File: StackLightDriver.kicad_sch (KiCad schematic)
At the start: 57 parts, among them J1 B2B-XH-A, J10 B2B-XH-A, J11 PJ-102AH, J2 B2B-XH-A, J3 B2B-XH-A, J4 B2B-XH-A, J5 B2B-XH-A, J6 B2B-XH-A, J7 B2B-XH-A, J8 B2B-XH-A, J9 B2B-XH-A, P1 282837-2, P2 282837-2, P3 282837-2, P4 282837-2, U6 ESP32-S3-WROOM-1-N4

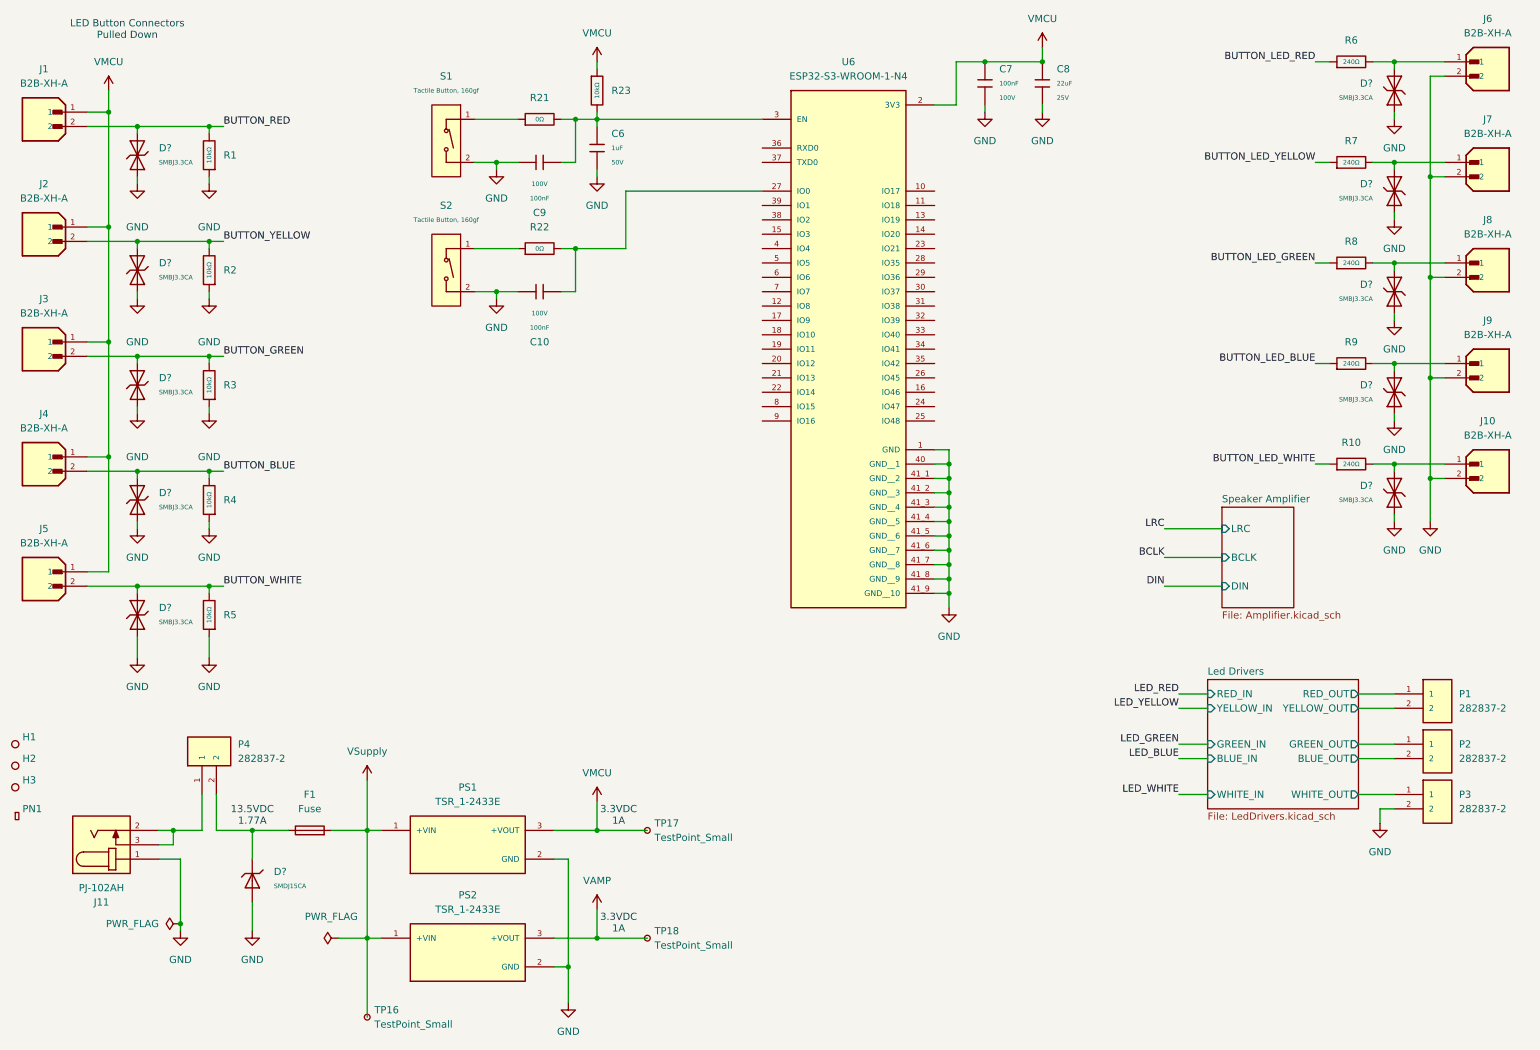
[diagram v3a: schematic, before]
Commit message: Rearranged ESP32 symbol, added note file
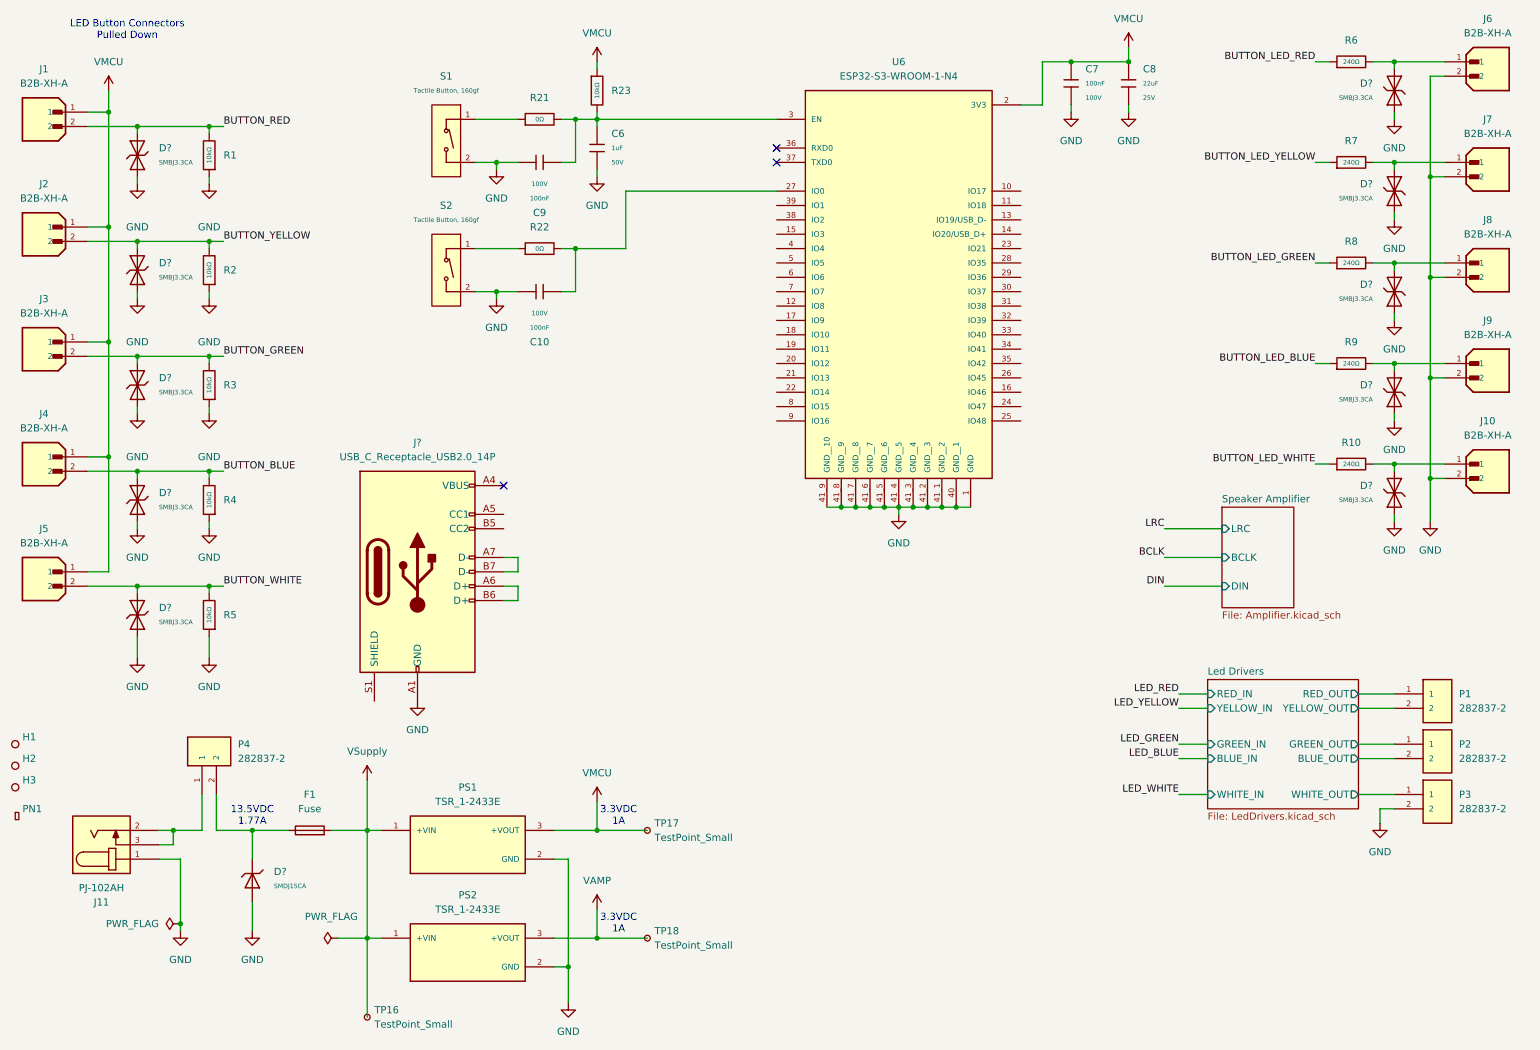
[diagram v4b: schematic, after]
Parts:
- added J?: USB_C_Receptacle_USB2.0_14P, symbol Connector:USB_C_Receptacle_USB2.0_14P
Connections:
- net GND: now also J?.A1 (GND), J?.A12 (GND), J?.B1 (GND), J?.B12 (GND)
- new net: J?.A4 (VBUS), J?.A9 (VBUS), J?.B4 (VBUS), J?.B9 (VBUS)
- new net: J?.A6 (D+), J?.B6 (D+)
- new net: J?.A7 (D-), J?.B7 (D-)
- no-connect marks 0 -> 3
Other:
- moved on the sheet: C7, C8, U6

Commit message: Added USB C connections and USB C TVS diodes
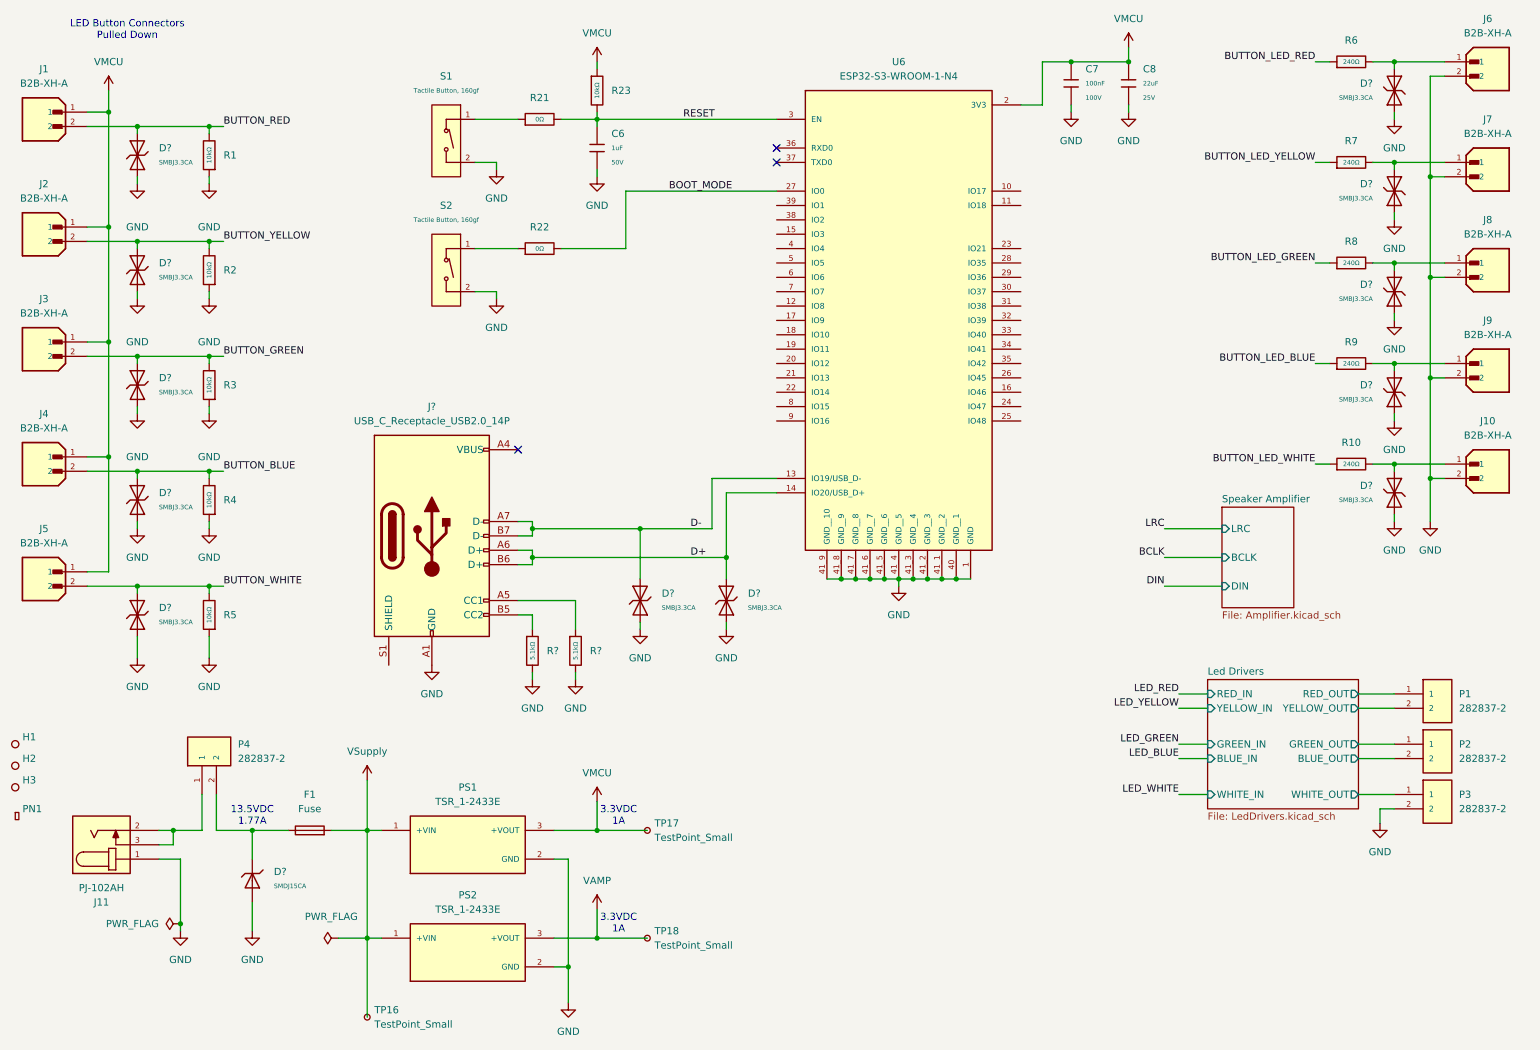
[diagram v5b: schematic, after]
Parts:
- removed C10, C9: 100nF, PCM_JLCPCB:C_0805, symbol PCM_JLCPCB-Capacitors:0805,100nF
- removed J?: USB_C_Receptacle_USB2.0_14P, symbol Connector:USB_C_Receptacle_USB2.0_14P
- added D? (x2): SMBJ3.3CA, PCM_JLCPCB:D_SMB, symbol PCM_JLCPCB-Diodes:TVS-Bi,SMBJ3.3CA
- added J?: USB_C_Receptacle_USB2.0_14P, symbol Project_symbols:USB_C_Receptacle_USB2.0_14P
- added R? (x2): 5.1kΩ, PCM_JLCPCB:R_0805, symbol PCM_JLCPCB-Resistors:0805,5.1kΩ
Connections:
- net GND: now also D?.1, D?.1, J?.A1 (GND), J?.A12 (GND), J?.B1 (GND), J?.B12 (GND), R?.2, R?.2
- net RESET: now reaches C6.1, R21.2, R23.2, U6.3 (EN)
- net D-: now reaches U6.13 (IO19/USB_D-)
- net D-: now also D?.2, J?.A7 (D-), J?.B7 (D-)
- net D+: now reaches U6.14 (IO20/USB_D+)
- net D+: now also D?.2, J?.A6 (D+), J?.B6 (D+)
- net BOOT_MODE: now reaches R22.2, U6.27 (IO0)
- new net: J?.A4 (VBUS), J?.A9 (VBUS), J?.B4 (VBUS), J?.B9 (VBUS)
- new net: J?.A5 (CC1), R?.1
- new net: J?.B5 (CC2), R?.1
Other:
- moved on the sheet: U6

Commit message: Added basic Littelfuse clip model, began laying out PCB
Still needs revisions to TVS diodes.
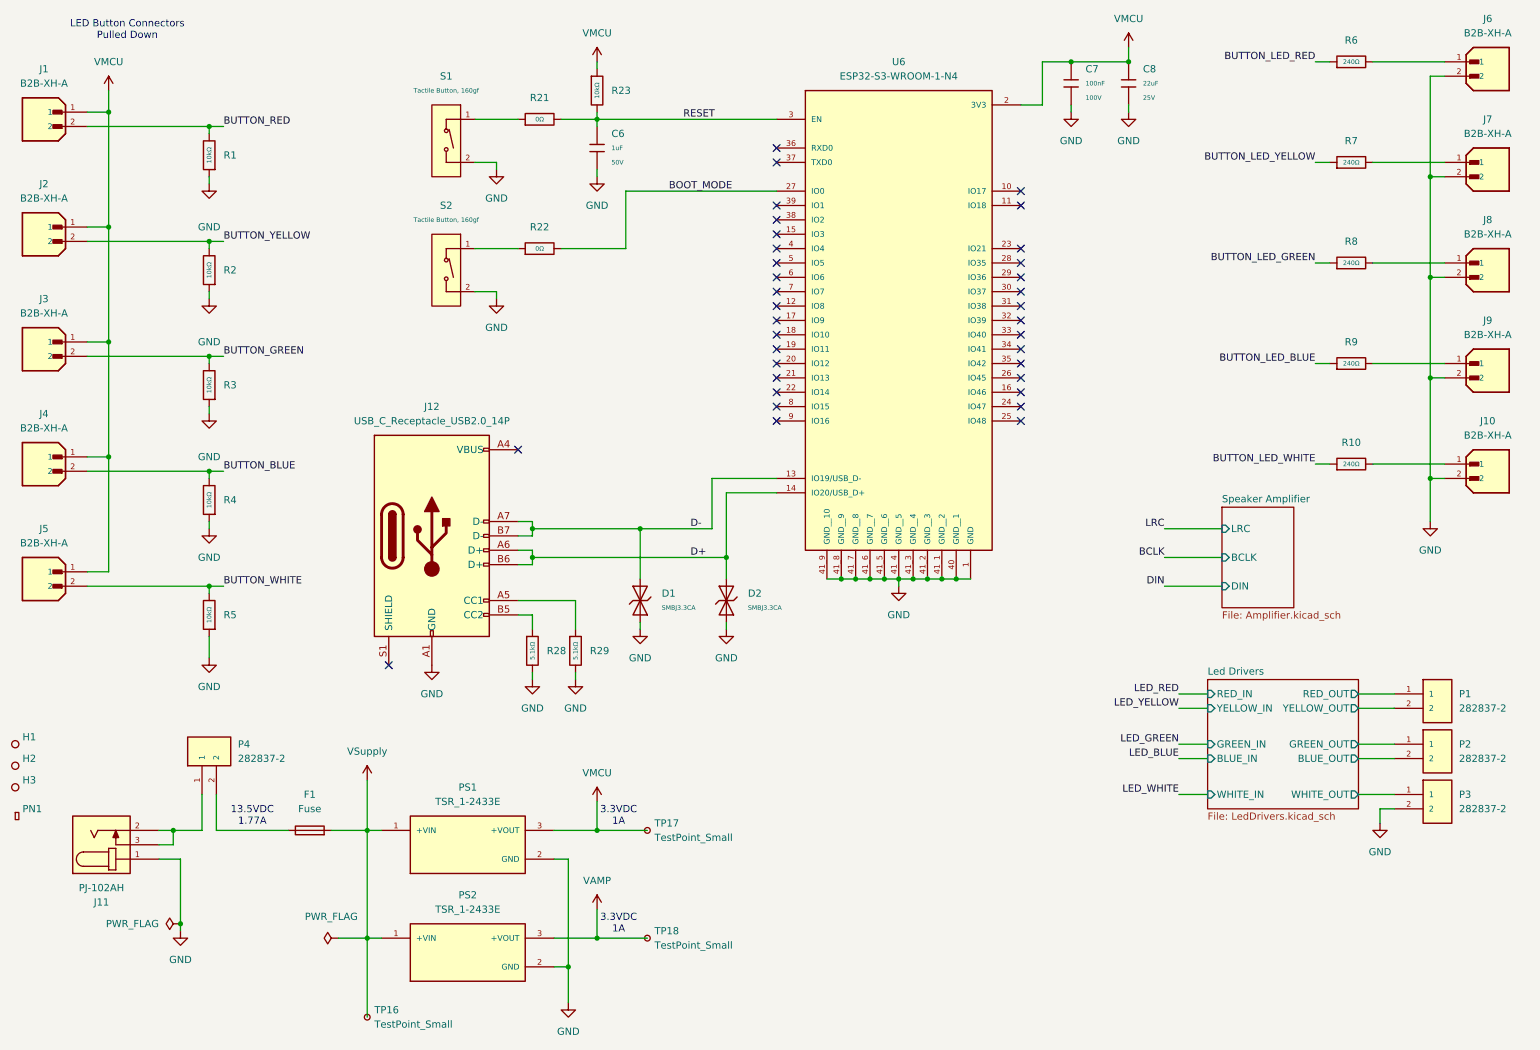
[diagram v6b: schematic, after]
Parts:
- removed D? (x10): SMBJ3.3CA, PCM_JLCPCB:D_SMB, symbol PCM_JLCPCB-Diodes:TVS-Bi,SMBJ3.3CA
- removed D?: SMDJ15CA, PCM_JLCPCB:D_SMC, symbol PCM_JLCPCB-Diodes:TVS-Uni,SMDJ15CA
- F1: footprint Fuse:Fuseholder_Clip-5x20mm_Littelfuse_111_Lateral_P18.80x5.00mm_D1.17mm_Horizontal -> Project_footprints:Fuseholder_Clip-5x20mm_Littelfuse_111_Lateral_P18.80x5.00mm_D1.17mm_Horizontal
- gave numbers to parts that had none: 5
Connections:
- no-connect marks 3 -> 35

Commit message: Added some TVS diodes to schematic and to PCB layout
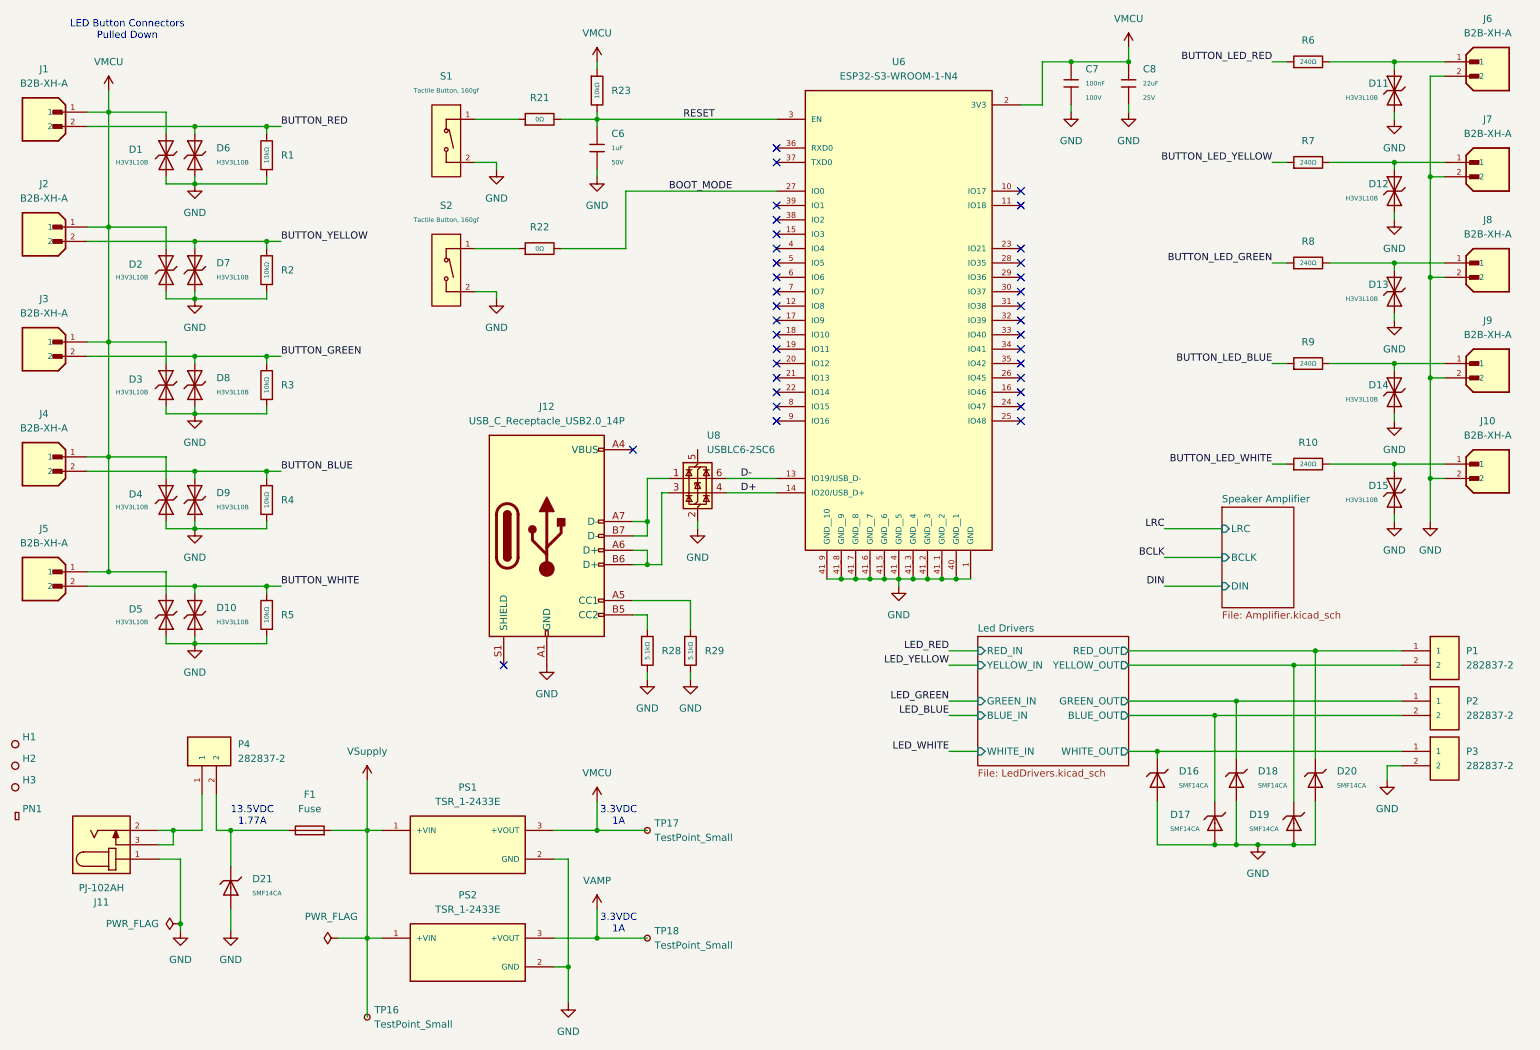
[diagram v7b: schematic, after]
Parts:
- removed D1, D2: SMBJ3.3CA, PCM_JLCPCB:D_SMB, symbol PCM_JLCPCB-Diodes:TVS-Bi,SMBJ3.3CA
- added D1, D10, D11, D12, D13, D14, D15, D2, D3, D4, D5, D6, D7, D8, D9: H3V3L10B, PCM_JLCPCB:D_DFN1006-2L, symbol PCM_JLCPCB-Diodes:TVS-Bi,H3V3L10B
- added D16, D17, D18, D19, D20, D21: SMF14CA, PCM_JLCPCB:D_SOD-123FL, symbol PCM_JLCPCB-Diodes:TVS-Uni,SMF14CA
- added U8: USBLC6-2SC6, Package_TO_SOT_SMD:SOT-23-6, symbol Power_Protection:USBLC6-2SC6
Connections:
- net BUTTON_BLUE: now also D9.2
- net BUTTON_GREEN: now also D8.2
- net BUTTON_RED: now also D6.2
- net BUTTON_WHITE: now also D10.2
- net BUTTON_YELLOW: now also D7.2
- net D+: now also U8.4 (I/O2); no longer J12.A6 (D+), J12.B6 (D+)
- net D-: now also U8.6 (I/O1); no longer J12.A7 (D-), J12.B7 (D-)
- net GND: now also D1.1, D10.1, D11.1, D12.1, D13.1, D14.1, D15.1, D16.2, D17.2, D18.2, D19.2, D2.1, D20.2, D21.2, D3.1, D4.1, D5.1, D6.1, D7.1, D8.1, D9.1, U8.2 (GND)
- net Led Drivers/BLUE_OUT: now also D17.1
- net Led Drivers/GREEN_OUT: now also D18.1
- net Led Drivers/RED_OUT: now also D20.1
- net Led Drivers/WHITE_OUT: now also D16.1
- net Led Drivers/YELLOW_OUT: now also D19.1
- net VMCU: now also D1.2, D2.2, D3.2, D4.2, D5.2
- net at J8.1, R8.2: now also D13.2
- net at F1.1, P4.2: now also D21.1
- net at J10.1, R10.2: now also D15.2
- net at J9.1, R9.2: now also D14.2
- net at J7.1, R7.2: now also D12.2
- net at J6.1, R6.2: now also D11.2
- new net: J12.A6 (D+), J12.B6 (D+), U8.3 (I/O2)
- new net: J12.A7 (D-), J12.B7 (D-), U8.1 (I/O1)
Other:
- moved on the sheet: J12, P1, P2, P3, R1, R10, R2, R28, R29, R3, R4, R5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
